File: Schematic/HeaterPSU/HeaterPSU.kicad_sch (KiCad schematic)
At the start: 48 parts, among them J201 SMPS2_SEC, J202 Heater Output, J203 Conn_01x06, Q201 IRF4905, SW201 SW_Rotary_1P5T_ALPSALPINE_SRBV, U201 TPS54302

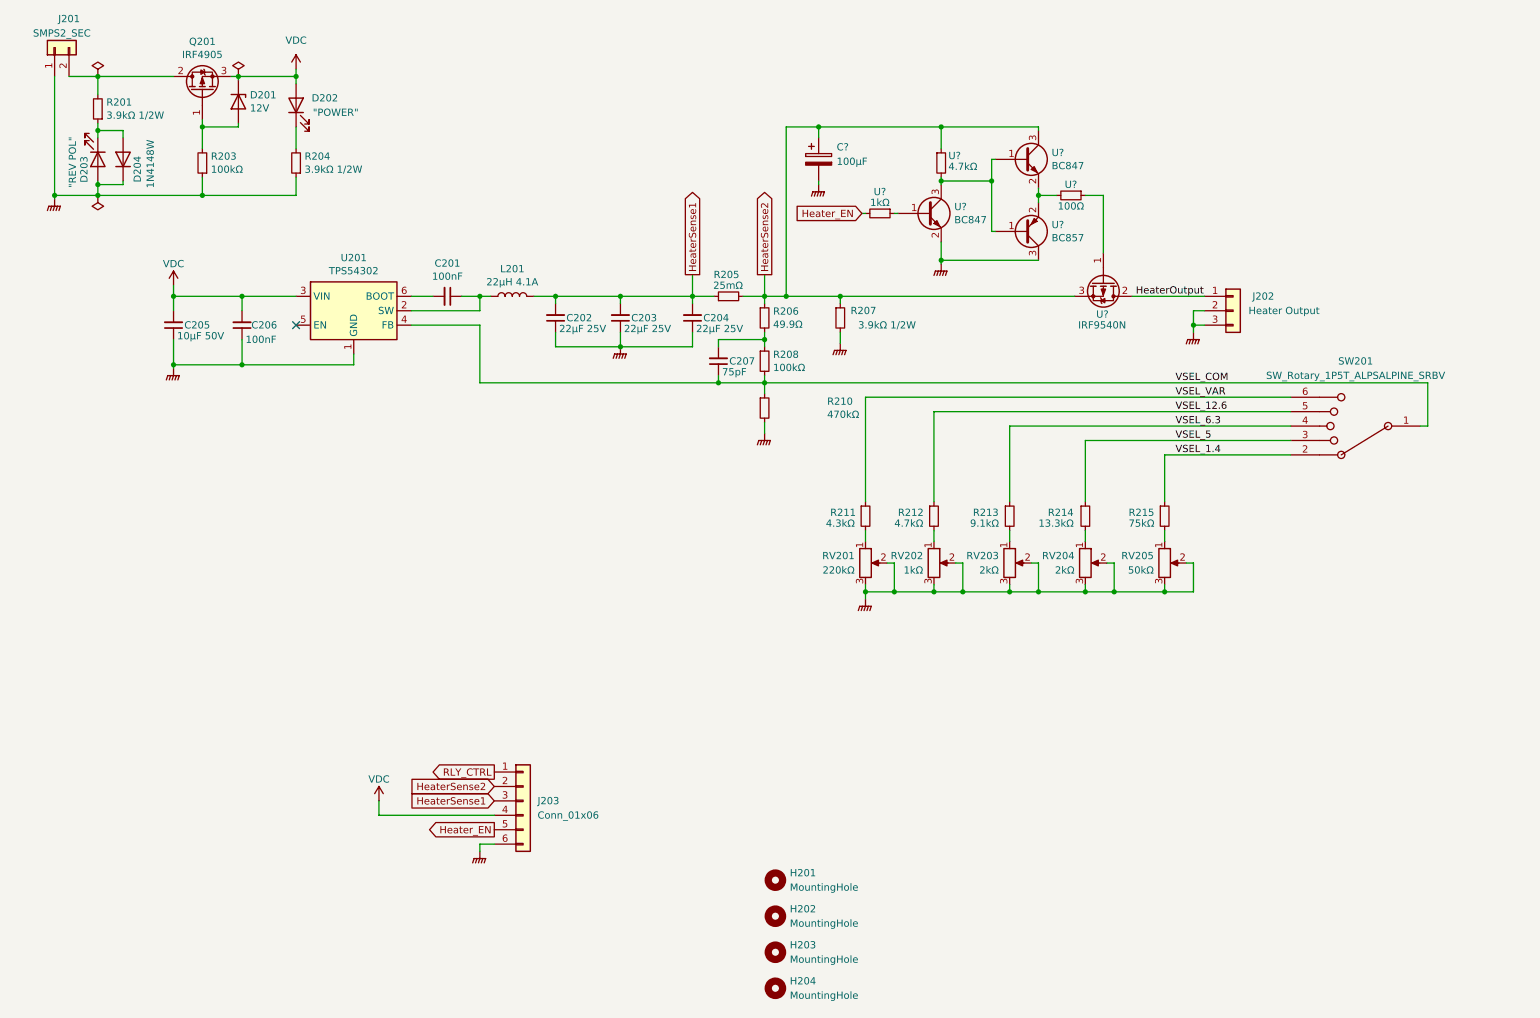
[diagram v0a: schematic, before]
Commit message: Added PWM controlled MOSFET output for soft start
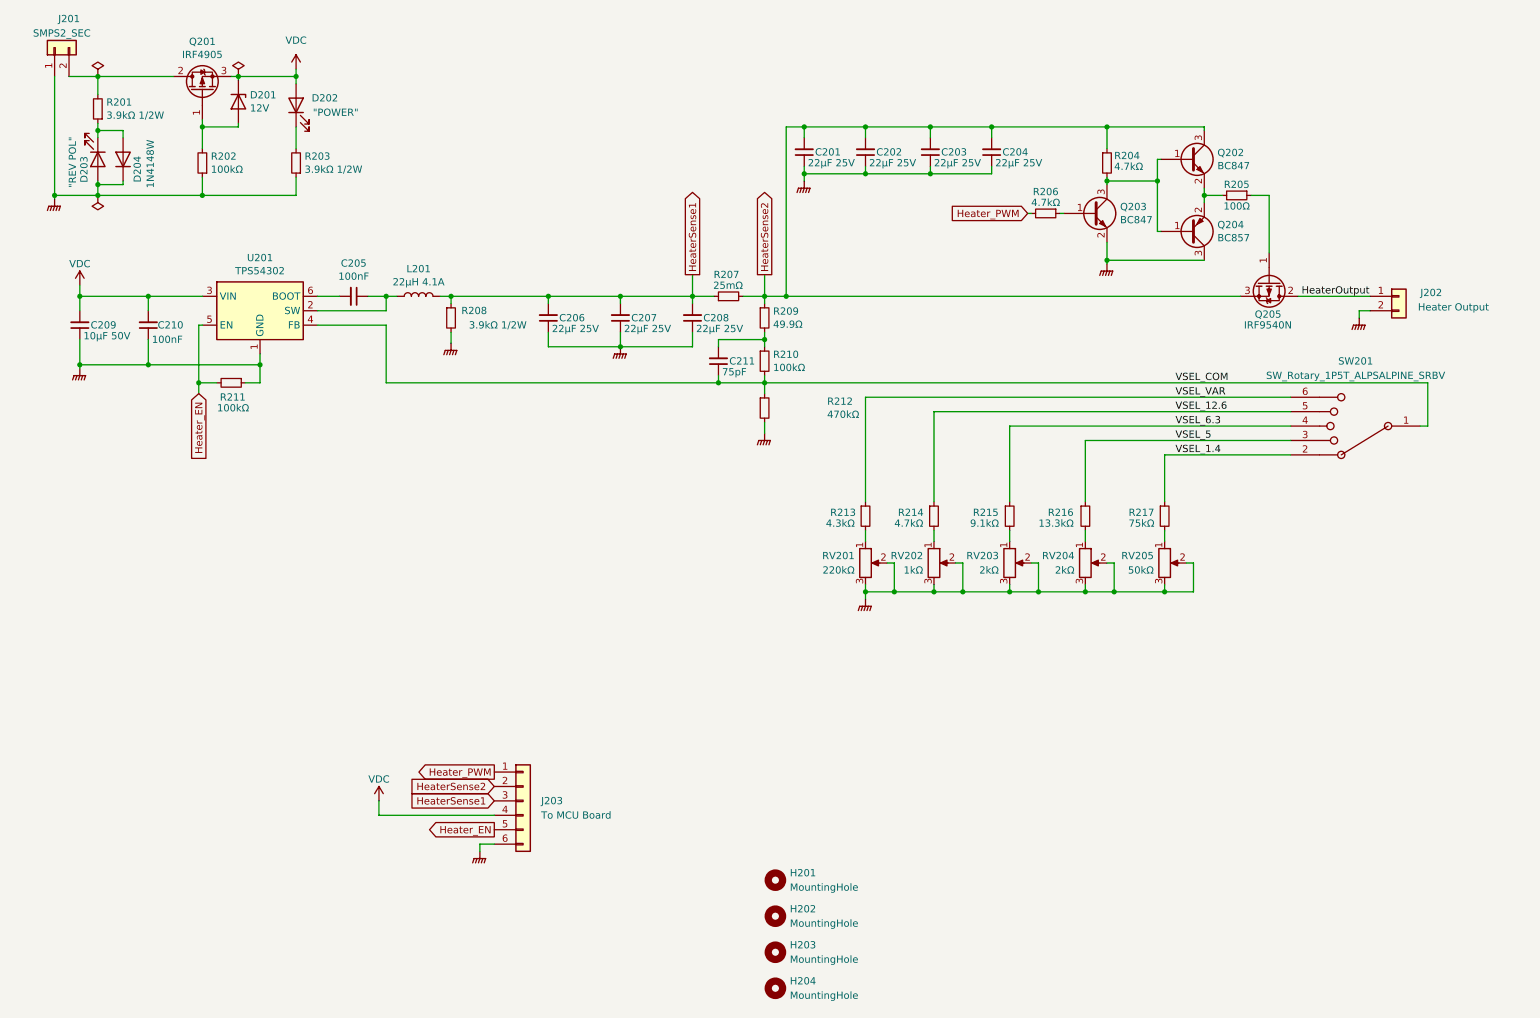
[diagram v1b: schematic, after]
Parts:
- removed C?: 100µF, symbol Device:C_Polarized
- added C201, C203, C204, C206: 22µF 25V, Capacitor_SMD:C_0805_2012Metric_Pad1.18x1.45mm_HandSolder, symbol Device:C_Small
- added R211: 100kΩ, Resistor_SMD:R_0805_2012Metric_Pad1.20x1.40mm_HandSolder, symbol Device:R_Small
- J202: footprint myDevices:TerminalBlock_LCSC_P5.08mm_3 -> myDevices:TerminalBlock_LCSC_P5.08mm; symbol Connector_Generic:Conn_01x03 -> Connector_Generic:Conn_01x02
- J203: value Conn_01x06 -> To MCU Board
- R204, R205: renamed from U?; footprint Resistor_SMD:R_0805_2012Metric_Pad1.15x1.40mm_HandSolder -> Resistor_SMD:R_0805_2012Metric_Pad1.20x1.40mm_HandSolder
- R206: renamed from U?; value 1kΩ -> 4.7kΩ; footprint Resistor_SMD:R_0805_2012Metric_Pad1.15x1.40mm_HandSolder -> Resistor_SMD:R_0805_2012Metric_Pad1.20x1.40mm_HandSolder
- gave numbers to parts that had none: 4
- renumbered C201 to C205, C203 to C207, C204 to C208, C205 to C209, C206 to C210, C207 to C211, R203 to R202, R204 to R203, R205 to R207, R207 to R208, R206 to R209, R208 to R210, R210 to R212, R211 to R213, R212 to R214, R213 to R215, R214 to R216, R215 to R217
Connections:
- net GNDPWR: now also C201.1, C203.1, C204.1, C206.1, R211.1; no longer J202.3 (Pin_3)
- net HeaterSense1: now also R208.1, C206.2; no longer C202.2
- net HeaterSense2: now also C202.2, C201.2, C203.2, C204.2; no longer R208.1
- net Heater_EN: now also U201.5 (EN), R211.2; no longer R206.2
- net RLY_CTRL renamed Heater_PWM
- net Heater_PWM: now also R206.2
- no-connect marks 1 -> 0
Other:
- moved on the sheet: C205, C209, C210, L201, Q202, Q203, Q204, Q205, R204, R205, R206, R208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

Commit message: Added 12V regulator for PWM output driver
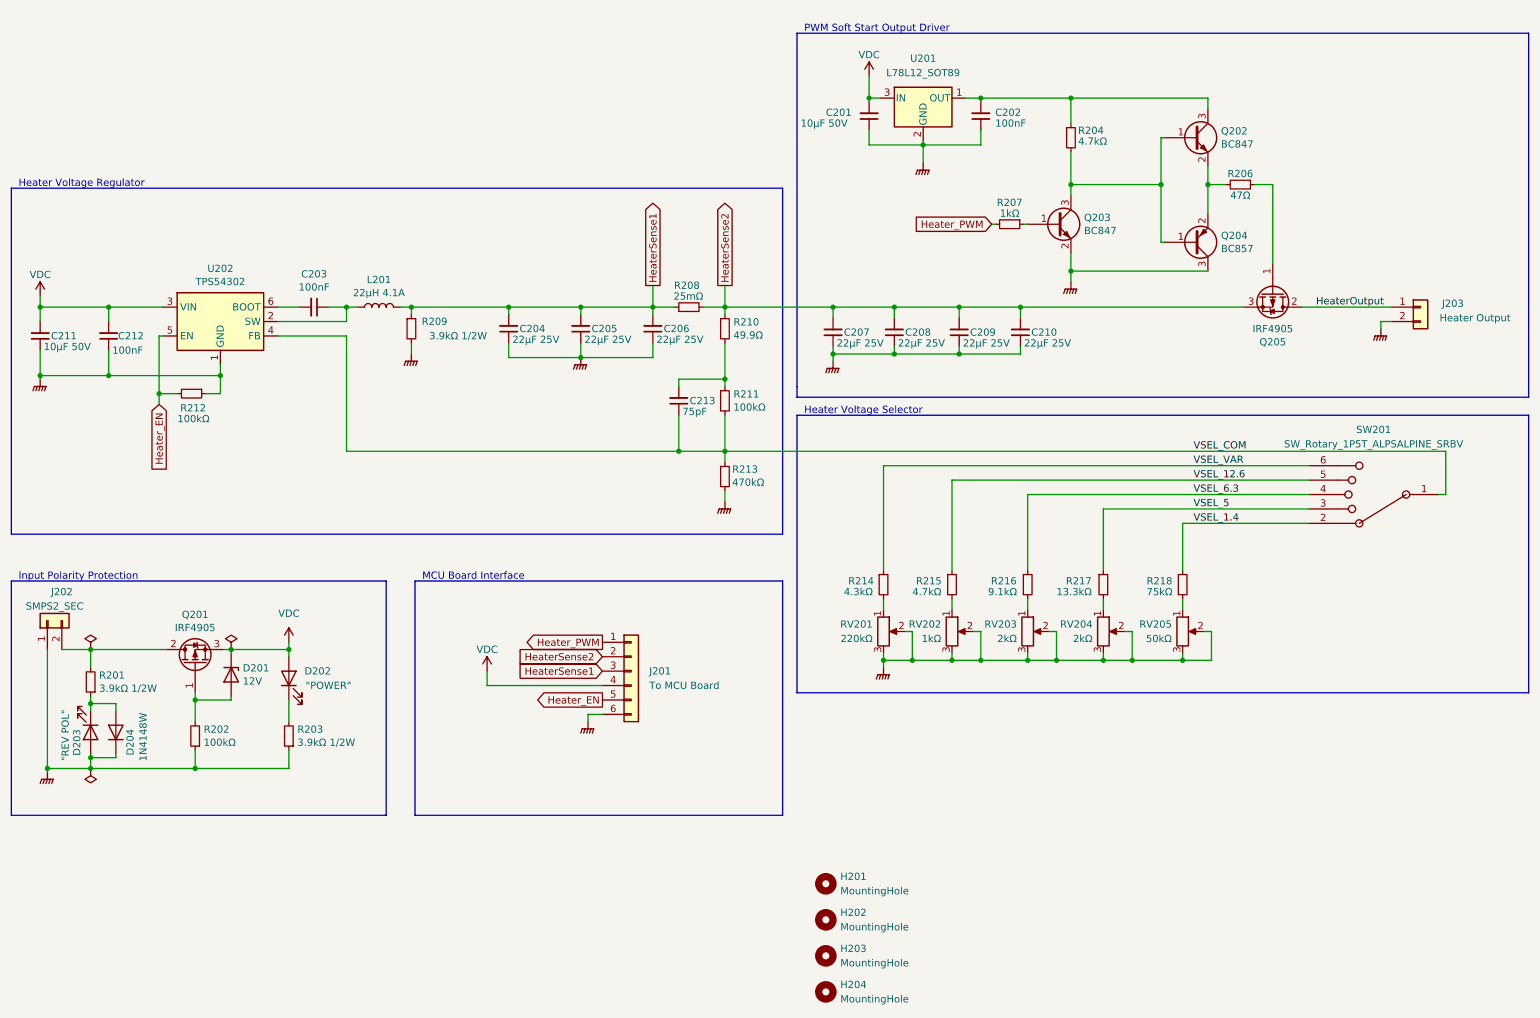
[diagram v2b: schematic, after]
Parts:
- removed Q205: IRF9540N, Package_TO_SOT_SMD:TO-263-2, symbol Transistor_FET:IRF9540N
- added C201: 10µF 50V, Capacitor_SMD:C_0805_2012Metric_Pad1.18x1.45mm_HandSolder, symbol Device:C_Small
- added C202: 100nF, Capacitor_SMD:C_0805_2012Metric_Pad1.18x1.45mm_HandSolder, symbol Device:C_Small
- added Q205: IRF4905, Package_TO_SOT_SMD:TO-263-2, symbol Transistor_FET:IRF4905
- added U201: L78L12_SOT89, Package_TO_SOT_SMD:SOT-89-3, symbol Regulator_Linear:L78L12_SOT89
- R206: renamed from R205; value 100Ω -> 47Ω
- R207: renamed from R206; value 4.7kΩ -> 1kΩ
- renumbered C205 to C203, C206 to C204, C207 to C205, C208 to C206, C201 to C207, C202 to C208, C203 to C209, C204 to C210, C209 to C211, C210 to C212, C211 to C213, J203 to J201, J201 to J202, J202 to J203, R207 to R208, R208 to R209, R209 to R210, R210 to R211, R211 to R212, R212 to R213, R213 to R214, R214 to R215, R215 to R216, R216 to R217, R217 to R218, U201 to U202
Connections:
- net GNDPWR: now also C201.1, C202.1, U201.2 (GND)
- net HeaterOutput: now also Q205.2 (D)
- net HeaterSense2: now also Q205.3 (S); no longer Q202.3 (C), R204.1
- net VDC: now also C201.2, U201.3 (IN)
- net at R206.1: now also Q205.1 (G)
- new net: C202.2, Q202.3 (C), R204.1, U201.1 (OUT)
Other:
- note added: "Heater Voltage Regulator"
- note added: "Heater Voltage Selector"
- note added: "Input Polarity Protection"
- note added: "MCU Board Interface"
- note added: "PWM Soft Start Output Driver"
- moved on the sheet: C203, C204, C205, C206, C207, C208, C209, C210, C211, C212, C213, D201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

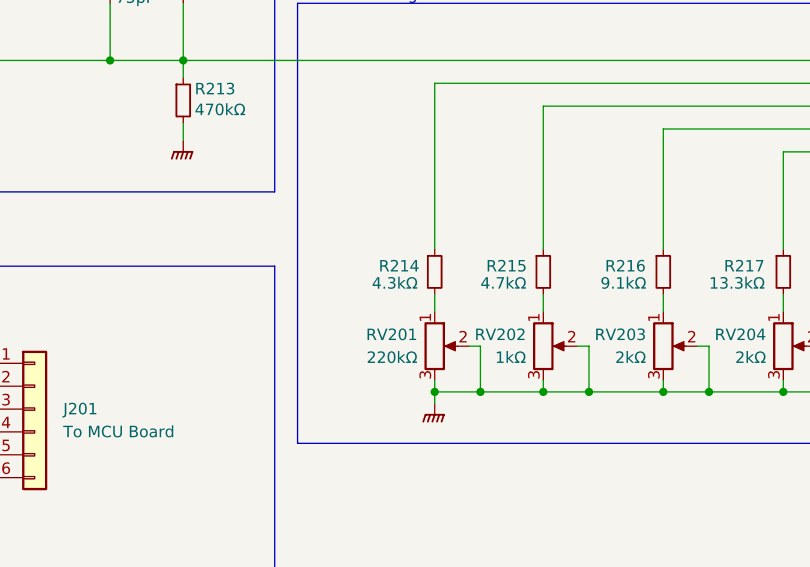
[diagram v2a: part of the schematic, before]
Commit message: Updated component values
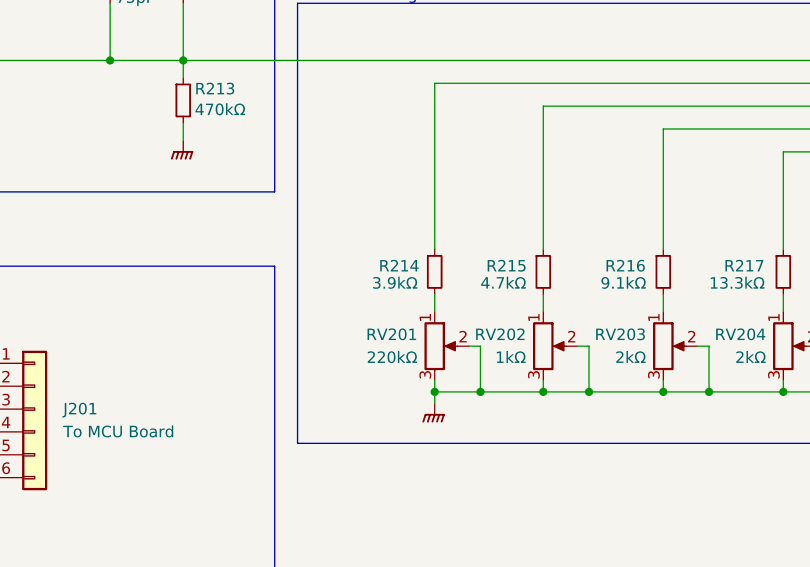
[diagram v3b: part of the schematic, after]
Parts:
- R214: value 4.3kΩ -> 3.9kΩ
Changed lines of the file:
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@@
       (effects (font (size 1.27 1.27)) (justify left))
     )
-    (property "Value" "4.3kΩ" (id 1) (at 160.02 118.11 0)
+    (property "Value" "3.9kΩ" (id 1) (at 160.02 118.11 0)
       (effects (font (size 1.27 1.27)) (justify left))
     )
@@
     )
     (path "/de1ddc97-c76c-452e-a2eb-b320798f7b28"
-      (reference "R214") (unit 1) (value "4.3kΩ") (footprint "Resistor_SMD:R_0805_2012Metric_Pad1.20x1.40mm_HandSolder")
+      (reference "R214") (unit 1) (value "3.9kΩ") (footprint "Resistor_SMD:R_0805_2012Metric_Pad1.20x1.40mm_HandSolder")
     )
     (path "/4a9313f8-9a6f-4a3f-98df-f7f3e11fea79"
